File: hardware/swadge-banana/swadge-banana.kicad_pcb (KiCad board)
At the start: 2 copper layers, 85 x 173.2 mm, 45 parts, among them J1 USB_B_Micro, SW1 SW_SPDT, U1 AP1117-33, U2 ESP-13-WROOM-02D, U3 BUS_PCIexpress, U4 OLED_CONNECTOR, U5 QMA6981, U6 OLED_DISPLAY

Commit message: Add plots and BOM
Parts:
- moved D5 2.17 mm to (118.1, 155.2), turned to 110 degrees
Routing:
- net GND: track 686.4 -> 731.4 mm, vias 43 -> 46
- net (no net): track 0.80 -> 11.2 mm
- net +3V3: track 616.8 -> 619.4 mm
- net Net-(D4-Pad2): track 42.9 -> 40.8 mm
- net Net-(D5-Pad2): track 33.9 -> 35.9 mm
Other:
- net class Default: clearance 0.2 -> 0.19
- net class Power: clearance 0.2 -> 0.19
- rule trace_clearance: 0.2 -> 0.19
- board text added: "swadge-banana-rev-"
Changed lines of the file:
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@@
   (general
     (thickness 1.6)
-    (drawings 262)
-    (tracks 1440)
+    (drawings 263)
+    (tracks 1473)
     (zones 0)
     (modules 45)
@@
     (user_trace_width 0.3)
     (user_trace_width 0.375)
-    (trace_clearance 0.2)
+    (trace_clearance 0.19)
     (zone_clearance 0.508)
     (zone_45_only no)
@@
     (pcbplotparams
       (layerselection 0x010fc_ffffffff)
-      (usegerberextensions false)
+      (usegerberextensions true)
       (usegerberattributes false)
       (usegerberadvancedattributes false)
@@
       (outputformat 1)
       (mirror false)
-      (drillshape 1)
+      (drillshape 0)
       (scaleselection 1)
-      (outputdirectory ""))
+      (outputdirectory "plots-rev_-"))
   )
   (net 0 "")
@@
   (net 38 "Net-(R4-Pad2)")
   (net_class Default "This is the default net class."
-    (clearance 0.2)
+    (clearance 0.19)
     (trace_width 0.25)
     (via_dia 0.8)
@@
   )
   (net_class Power ""
-    (clearance 0.2)
+    (clearance 0.19)
     (trace_width 0.4)
     (via_dia 0.8)
@@
   )
   (module Swadge_Parts:LED_WS2812B_PLCC4_5.0x5.0mm_P3.2mm (layer F.Cu)
-    (at 118.68 157.33 113)
+    (at 118.075 155.25 110)
     (descr https://cdn-shop.adafruit.com/datasheets/WS2812B.pdf)
     (tags "LED RGB NeoPixel")
     (attr smd)
-    (fp_text reference D5 (at -6.17856 -1.10717 113) (layer F.SilkS)
+    (fp_text reference D5 (at -6.17856 -1.10717 110) (layer F.SilkS)
       (effects (font (size 1 1) (thickness 0.15)))
     )
-    (fp_text value WS2812B (at 0.000001 4 113) (layer F.SilkS)
+    (fp_text value WS2812B (at 0.000001 4 110) (layer F.SilkS)
       (effects (font (size 1 1) (thickness 0.15)))
     )
@@
     (fp_line (start 3.45 2.75) (end 3.45 -2.75) (layer F.CrtYd) (width 0.05))
     (fp_line (start 3.45 -2.75) (end -3.45 -2.75) (layer F.CrtYd) (width 0.05))
-    (fp_text user %R (at 0 0 113) (layer F.Fab)
+    (fp_text user %R (at 0 0 110) (layer F.Fab)
       (effects (font (size 0.8 0.8) (thickness 0.15)))
     )
-    (fp_text user 1 (at -4.15 -1.6 113) (layer F.SilkS)
+    (fp_text user 1 (at -4.15 -1.6 110) (layer F.SilkS)
       (effects (font (size 1 1) (thickness 0.15)))
     )
-    (pad 1 smd rect (at -2.45 -1.6 113) (size 1.5 1) (layers F.Cu F.Paste F.Mask)
+    (pad 1 smd rect (at -2.45 -1.6 110) (size 1.5 1) (layers F.Cu F.Paste F.Mask)
       (net 32 +3V3))
-    (pad 2 smd rect (at -2.45 1.6 113) (size 1.5 1) (layers F.Cu F.Paste F.Mask)
+    (pad 2 smd rect (at -2.45 1.6 110) (size 1.5 1) (layers F.Cu F.Paste F.Mask)
       (net 11 "Net-(D5-Pad2)"))
-    (pad 4 smd rect (at 2.45 -1.6 113) (size 1.5 1) (layers F.Cu F.Paste F.Mask)
+    (pad 4 smd rect (at 2.45 -1.6 110) (size 1.5 1) (layers F.Cu F.Paste F.Mask)
       (net 10 "Net-(D4-Pad2)"))
-    (pad 3 smd rect (at 2.45 1.6 113) (size 1.5 1) (layers F.Cu F.Paste F.Mask)
+    (pad 3 smd rect (at 2.45 1.6 110) (size 1.5 1) (layers F.Cu F.Paste F.Mask)
       (net 31 GND))
     (model ${KIPRJMOD}/../kicad-libs/package3d/WS2812_RGB_LED_updated.stp
@@
     )
   )
+  (gr_text swadge-banana-rev- (at 132.588 103.124 80) (layer B.SilkS)
+    (effects (font (size 1 1) (thickness 0.15)) (justify mirror))
+  )
   (gr_line (start 190.827837 18.988906) (end 190.616677 18.788795) (layer Edge.Cuts) (width 0.132291))
   (gr_line (start 189.988306 18.268913) (end 189.573984 17.983371) (layer Edge.Cuts) (width 0.132291))
@@
   (gr_line (start 170.5102 46.99) (end 172.423756 43.591814) (layer Edge.Cuts) (width 0.132291))
   (segment (start 132.025 123.05) (end 131.275 123.325) (width 0.25) (layer F.Cu) (net 0))
+  (segment (start 118.872 87.884) (end 118.872 87.376) (width 0.25) (layer F.Cu) (net 0))
+  (segment (start 118.872 87.376) (end 119.38 86.868) (width 0.25) (layer F.Cu) (net 0))
+  (segment (start 119.38 86.868) (end 120.396 86.868) (width 0.25) (layer F.Cu) (net 0))
+  (segment (start 120.396 86.868) (end 119.888 86.36) (width 0.25) (layer F.Cu) (net 0))
+  (segment (start 119.888 86.36) (end 119.888 87.376) (width 0.25) (layer F.Cu) (net 0))
+  (segment (start 119.888 87.376) (end 119.38 87.884) (width 0.25) (layer F.Cu) (net 0))
+  (segment (start 119.38 87.884) (end 118.872 87.884) (width 0.25) (layer F.Cu) (net 0))
+  (segment (start 119.888 86.36) (end 119.888 87.376) (width 0.25) (layer B.Cu) (net 0))
+  (segment (start 119.888 87.376) (end 119.38 87.884) (width 0.25) (layer B.Cu) (net 0))
+  (segment (start 119.38 87.884) (end 118.872 87.884) (width 0.25) (layer B.Cu) (net 0))
+  (segment (start 118.872 87.884) (end 118.872 87.376) (width 0.25) (layer B.Cu) (net 0))
+  (segment (start 118.872 87.376) (end 119.38 86.868) (width 0.25) (layer B.Cu) (net 0))
+  (segment (start 119.38 86.868) (end 120.396 86.868) (width 0.25) (layer B.Cu) (net 0))
+  (segment (start 120.396 86.868) (end 119.888 86.36) (width 0.25) (layer B.Cu) (net 0))
   (segment (start 133.216699 124.157737) (end 141.331354 81.806096) (width 0.45) (layer F.Cu) (net 1))
   (segment (start 133.216699 124.157737) (end 141.331354 81.806096) (width 0.45) (layer B.Cu) (net 1))
@@
   (segment (start 112.15 116.85) (end 111.725 117.6) (width 0.25) (layer F.Cu) (net 9))
   (segment (start 111.725 117.6) (end 110.87397 117.637095) (width 0.25) (layer F.Cu) (net 9))
-  (segment (start 116.249901 155.699933) (end 115.375 153.775) (width 0.25) (layer F.Cu) (net 10))
   (segment (start 115.375 153.775) (end 114.925 151.725) (width 0.25) (layer F.Cu) (net 10))
   (segment (start 114.925 151.725) (end 114.15 149.3) (width 0.25) (layer F.Cu) (net 10))
@@
   (segment (start 121.95 159.875) (end 121.725 159.8) (width 0.25) (layer F.Cu) (net 11))
   (segment (start 121.725 159.8) (end 121.110099 158.960067) (width 0.25) (layer F.Cu) (net 11))
+  (segment (start 121.05 158.85) (end 120.066458 157.105015) (width 0.25) (layer F.Cu) (net 11))
   (segment (start 146.09 186.205) (end 146.175 183.6) (width 0.25) (layer F.Cu) (net 12))
   (segment (start 146.175 183.6) (end 145.75 182.525) (width 0.25) (layer F.Cu) (net 12))
@@
   (segment (start 128.825 146.825) (end 130.725 145.75) (width 0.25) (layer F.Cu) (net 31))
   (segment (start 130.001651 171.509499) (end 124.935082 166.778309) (width 0.25) (layer F.Cu) (net 31))
-  (segment (start 119.195517 154.449593) (end 121.075 154.3) (width 0.25) (layer F.Cu) (net 31))
   (segment (start 121.075 154.3) (end 124.936748 153.725536) (width 0.25) (layer F.Cu) (net 31))
   (via (at 120.575 79.875) (size 0.8) (drill 0.4) (layers F.Cu B.Cu) (net 31))
@@
   (via (at 125.1966 171.0436) (size 0.8) (drill 0.4) (layers F.Cu B.Cu) (net 31))
   (via (at 126.4412 164.0332) (size 0.8) (drill 0.4) (layers F.Cu B.Cu) (net 31))
+  (segment (start 119.175 88.775) (end 117.348 88.392) (width 0.25) (layer B.Cu) (net 31))
+  (segment (start 117.348 88.392) (end 116.332 86.868) (width 0.25) (layer B.Cu) (net 31))
+  (segment (start 116.332 86.868) (end 113.5634 86.6648) (width 0.25) (layer B.Cu) (net 31))
+  (segment (start 118.740559 152.400521) (end 119.928768 154.391232) (width 0.25) (layer F.Cu) (net 31))
+  (segment (start 119.195517 154.449593) (end 119.928768 154.391232) (width 0.25) (layer F.Cu) (net 31))
+  (segment (start 119.928768 154.391232) (end 121.075 154.3) (width 0.25) (layer F.Cu) (net 31))
+  (segment (start 126.4412 164.0332) (end 123.952 163.576) (width 0.25) (layer B.Cu) (net 31))
+  (via (at 123.444 163.576) (size 0.8) (drill 0.4) (layers F.Cu B.Cu) (net 31))
+  (segment (start 123.952 163.576) (end 123.444 163.576) (width 0.25) (layer B.Cu) (net 31))
+  (segment (start 123.444 163.576) (end 124.935082 166.778309) (width 0.25) (layer F.Cu) (net 31))
+  (segment (start 125.1966 171.0436) (end 129.525 168.7) (width 0.25) (layer B.Cu) (net 31))
+  (via (at 140.716 45.72) (size 0.8) (drill 0.4) (layers F.Cu B.Cu) (net 31))
+  (segment (start 136.8044 40.8432) (end 140.716 45.72) (width 0.25) (layer B.Cu) (net 31))
+  (segment (start 140.716 45.72) (end 133.577264 48.581247) (width 0.25) (layer F.Cu) (net 31))
+  (via (at 122.936 71.12) (size 0.8) (drill 0.4) (layers F.Cu B.Cu) (net 31))
+  (segment (start 118.6434 69.4182) (end 122.936 71.12) (width 0.25) (layer B.Cu) (net 31))
+  (segment (start 122.936 71.12) (end 122.590008 66.169341) (width 0.25) (layer F.Cu) (net 31))
+  (segment (start 121.953814 148.178814) (end 121.222336 149.158548) (width 0.25) (layer F.Cu) (net 31))
   (segment (start 184.475536 28.663252) (end 185.55 25.525) (width 0.25) (layer F.Cu) (net 32) (status 10))
   (segment (start 185.55 25.525) (end 184.685481 23.163416) (width 0.25) (layer F.Cu) (net 32) (status 20))
@@
   (segment (start 119.775 165.025) (end 117.738899 161.061101) (width 0.25) (layer F.Cu) (net 32))
   (segment (start 118.164483 160.210407) (end 117.738899 161.061101) (width 0.25) (layer F.Cu) (net 32))
-  (segment (start 117.738899 161.061101) (end 117.425 160.45) (width 0.25) (layer F.Cu) (net 32))
   (segment (start 149.651337 101.326337) (end 149.5 101.85) (width 0.25) (layer F.Cu) (net 32))
   (segment (start 153.9 86.625) (end 149.651337 101.326337) (width 0.25) (layer F.Cu) (net 32))
@@
   (segment (start 119.671264 147.421264) (end 119.671264 148.885052) (width 0.25) (layer F.Cu) (net 32))
   (segment (start 119.35 147.1) (end 119.671264 147.421264) (width 0.25) (layer F.Cu) (net 32))
+  (segment (start 117.059441 158.199479) (end 117.543773 160.681227) (width 0.25) (layer F.Cu) (net 32))
+  (segment (start 117.738899 161.061101) (end 117.543773 160.681227) (width 0.25) (layer F.Cu) (net 32))
+  (segment (start 117.543773 160.681227) (end 117.425 160.45) (width 0.25) (layer F.Cu) (net 32))
   (via (at 154.95 182.9) (size 0.8) (drill 0.4) (layers F.Cu B.Cu) (net 33))
   (segment (start 155.09 186.205) (end 154.95 182.9) (width 0.45) (layer B.Cu) (net 33))

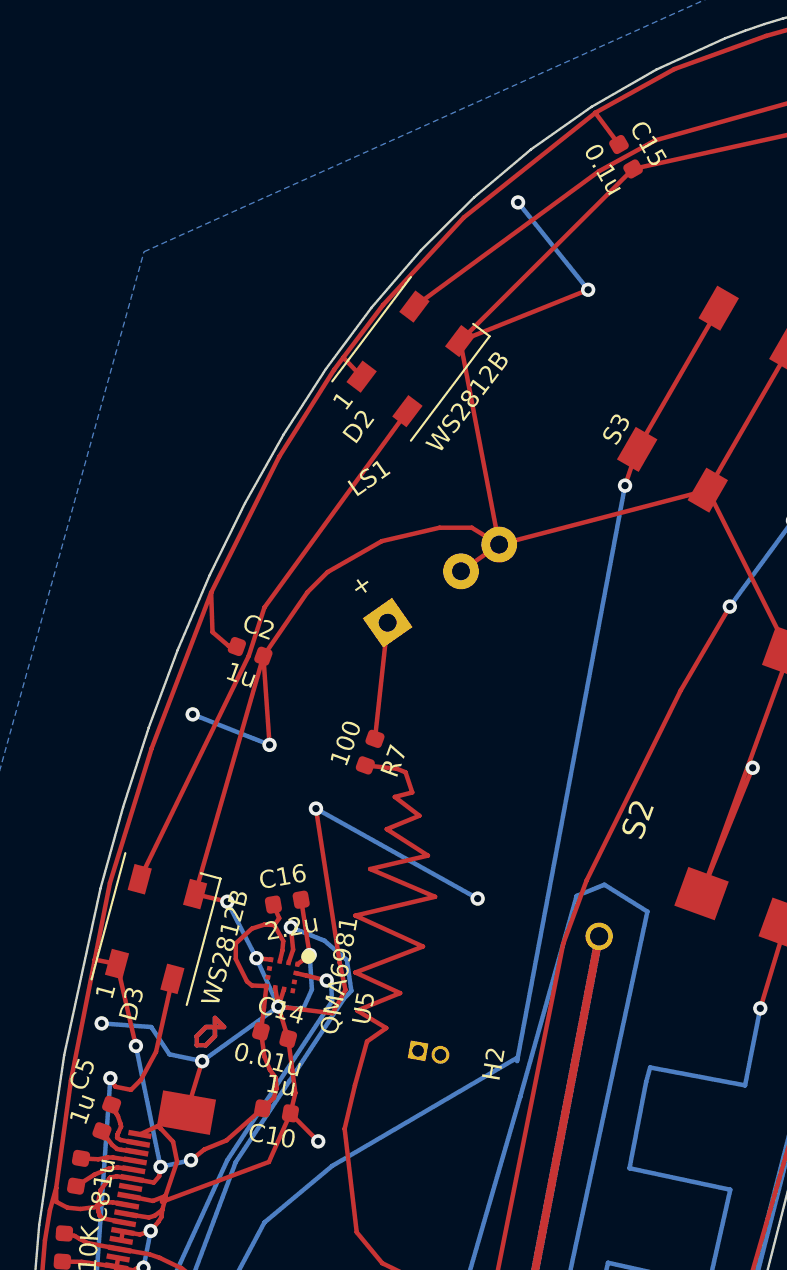
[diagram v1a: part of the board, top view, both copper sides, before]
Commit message: Properly aligned accelerometer Moved C15 closer to accelerometer
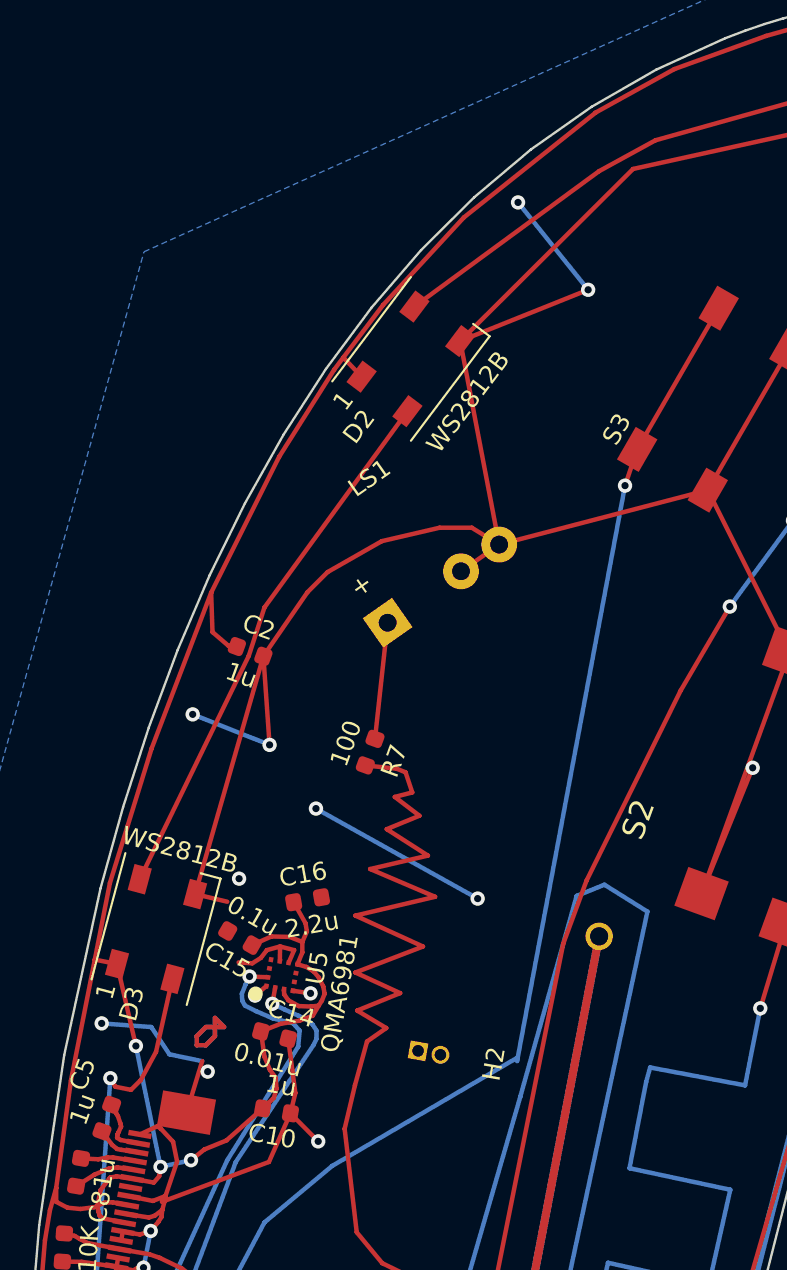
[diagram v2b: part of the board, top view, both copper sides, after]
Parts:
- moved C15 48.6 mm to (121.3, 81.9), turned to 150 degrees
- moved C16 1.14 mm to (125.1, 79.8)
- turned U5 to 80 degrees
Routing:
- net GND: track 731.4 -> 698.4 mm, vias 46 -> 45
- net SDA: track 156.9 -> 150.4 mm
- net +3V3: track 619.4 -> 621.2 mm
- net SCL: track 124.8 -> 125.7 mm

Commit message: Bump to Rev A with Adam's change
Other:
- board text added: "swadge-banana-revA"
- board text removed: "swadge-banana-rev-"
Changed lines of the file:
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@@
-(kicad_pcb (version 20171130) (host pcbnew "(5.1.2)-2")
+(kicad_pcb (version 20171130) (host pcbnew 5.1.3-ffb9f22~84~ubuntu18.04.1)
   (general
     (thickness 1.6)
@@
       (drillshape 0)
       (scaleselection 1)
-      (outputdirectory "plots-rev_-"))
+      (outputdirectory "plots-rev_A"))
   )
   (net 0 "")
@@
     )
   )
-  (gr_text swadge-banana-rev- (at 132.588 103.124 80) (layer B.SilkS)
+  (gr_text swadge-banana-revA (at 132.588 103.124 80) (layer B.SilkS)
     (effects (font (size 1 1) (thickness 0.15)) (justify mirror))
   )

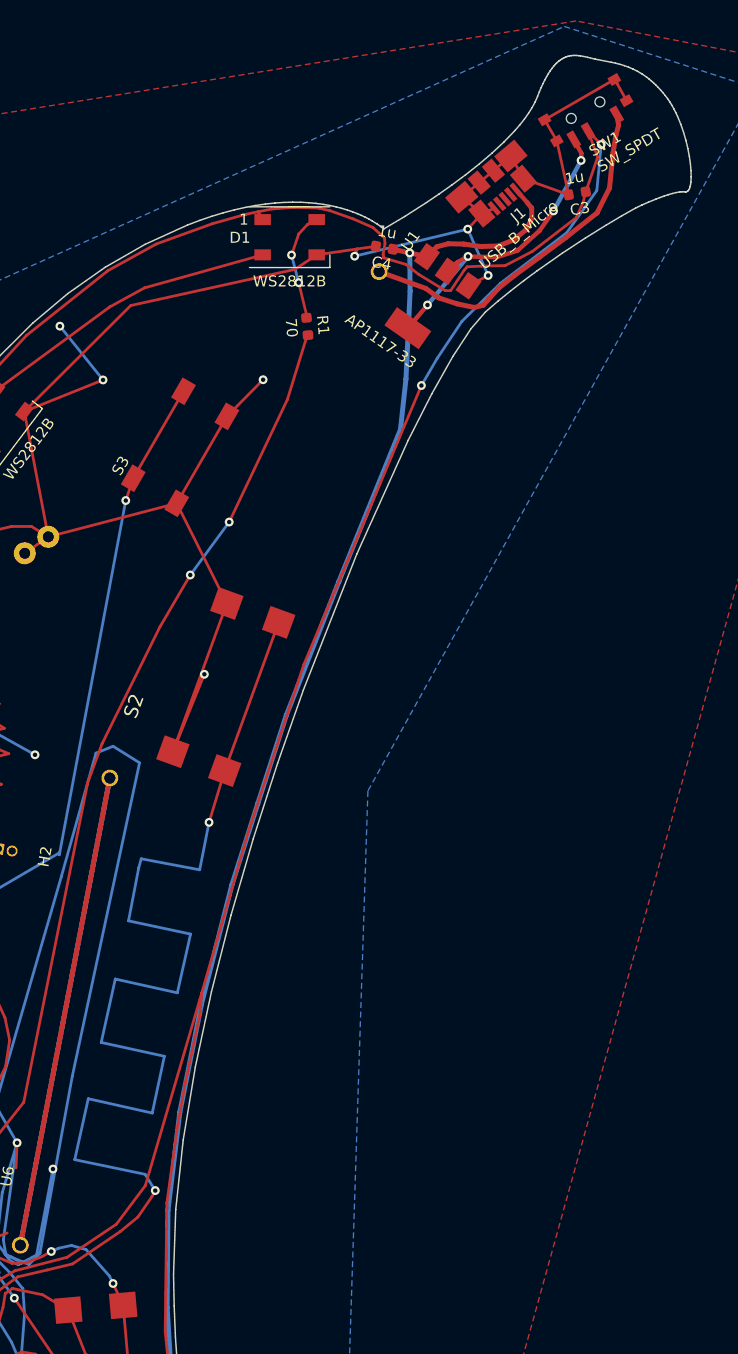
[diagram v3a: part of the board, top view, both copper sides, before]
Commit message: Added & Updated silkscreen  * Labeled buttons, power switch  * Labeled PCIe connector  * Added funkus & logo graphics  * Added note that USB is power only  * Added instruction URL  * Updated revision
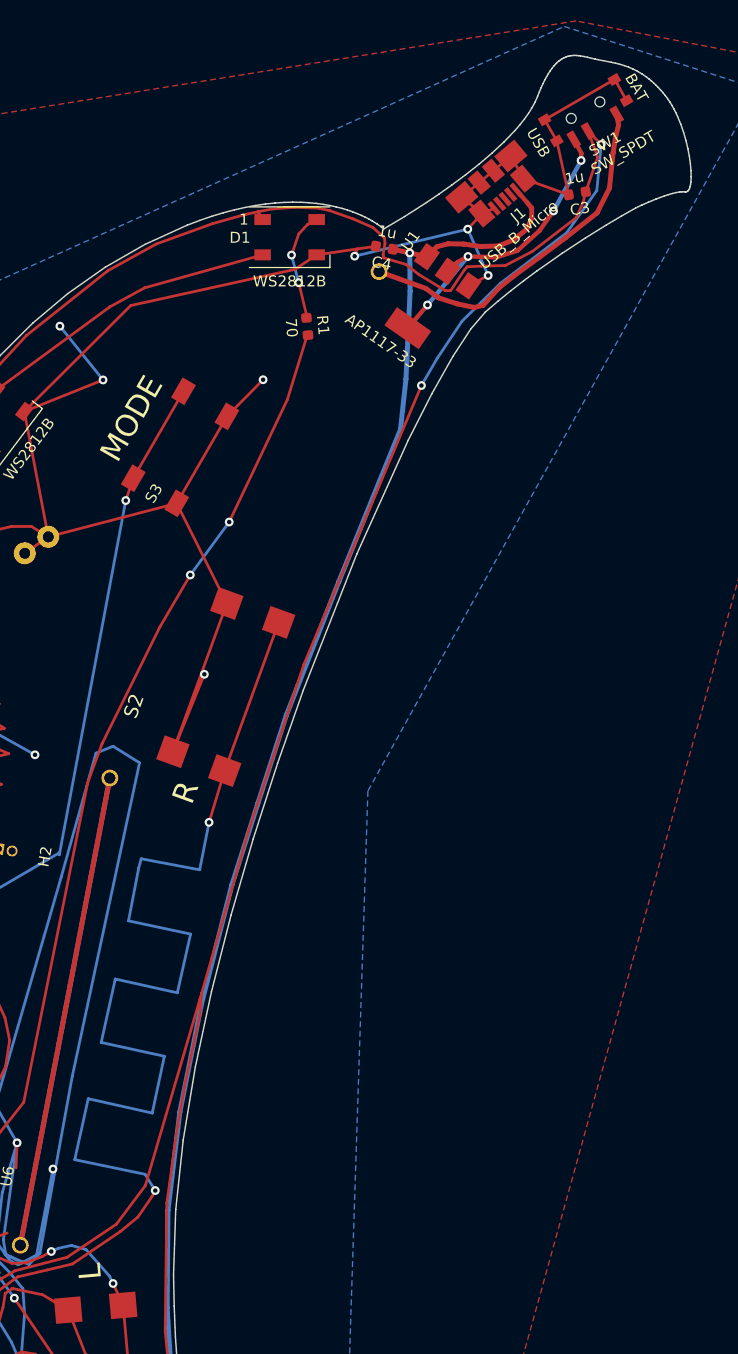
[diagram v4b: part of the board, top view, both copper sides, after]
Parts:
- added G***: LOGO, Swadge_Parts:funkus, B.Cu at (125.3, 101.6)
- added G***: LOGO, Swadge_Parts:mag-logo-outline, B.Cu at (120.7, 143.8)
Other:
- board text added: "3.3V"
- board text added: "5V"
- board text added: "BAT"
- board text added: "BZR"
- board text added: "G14"
- board text added: "GND"
- board text added: "Instructions at http://swadge.com/super2020/"
- board text added: "L"
- board text added: "LED"
- board text added: "MODE"
- board text added: "PWR ONLY"
- board text added: "R"
- board text added: "REST"
- board text added: "RX"
- board text added: "S1"
- board text added: "S2"
- board text added: "S3"
- board text added: "SCL"
- board text added: "SDA"
- board text added: "Swadge 2020 Banana revB"
- board text added: "TOUT"
- board text added: "TX"
- board text added: "USB"
- board text added: "_RES"
- board text removed: "swadge-banana-revA"

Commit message: Rotated banana text to be consistent
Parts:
- turned G*** to 280 degrees
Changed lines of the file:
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@@
   (page A4)
   (layers
-    (0 F.Cu signal)
+    (0 F.Cu signal hide)
     (31 B.Cu signal)
-    (32 B.Adhes user)
-    (33 F.Adhes user)
+    (32 B.Adhes user hide)
+    (33 F.Adhes user hide)
     (34 B.Paste user)
-    (35 F.Paste user)
+    (35 F.Paste user hide)
     (36 B.SilkS user)
-    (37 F.SilkS user)
+    (37 F.SilkS user hide)
     (38 B.Mask user)
-    (39 F.Mask user)
-    (40 Dwgs.User user)
-    (41 Cmts.User user)
-    (42 Eco1.User user)
-    (43 Eco2.User user)
+    (39 F.Mask user hide)
+    (40 Dwgs.User user hide)
+    (41 Cmts.User user hide)
+    (42 Eco1.User user hide)
+    (43 Eco2.User user hide)
     (44 Edge.Cuts user)
-    (45 Margin user)
+    (45 Margin user hide)
     (46 B.CrtYd user)
-    (47 F.CrtYd user)
+    (47 F.CrtYd user hide)
     (48 B.Fab user)
-    (49 F.Fab user)
+    (49 F.Fab user hide)
   )
   (setup
@@
   )
   (module Swadge_Parts:mag-logo-outline (layer B.Cu)
-    (at 120.65 143.75 100)
+    (at 120.65 143.75 280)
     (fp_text reference G*** (at 0 0 100) (layer B.SilkS) hide
       (effects (font (size 1.524 1.524) (thickness 0.3)) (justify mirror))
@@
     )
   )
-  (gr_text "PWR ONLY" (at 175.75 27.475 220) (layer B.SilkS)
+  (gr_text "PWR ONLY" (at 175.75 27.475 40) (layer B.SilkS)
     (effects (font (size 1 1) (thickness 0.15)) (justify mirror))
   )
